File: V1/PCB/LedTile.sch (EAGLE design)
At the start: 71 parts, among them U1 BME280, U2 TSL2561T

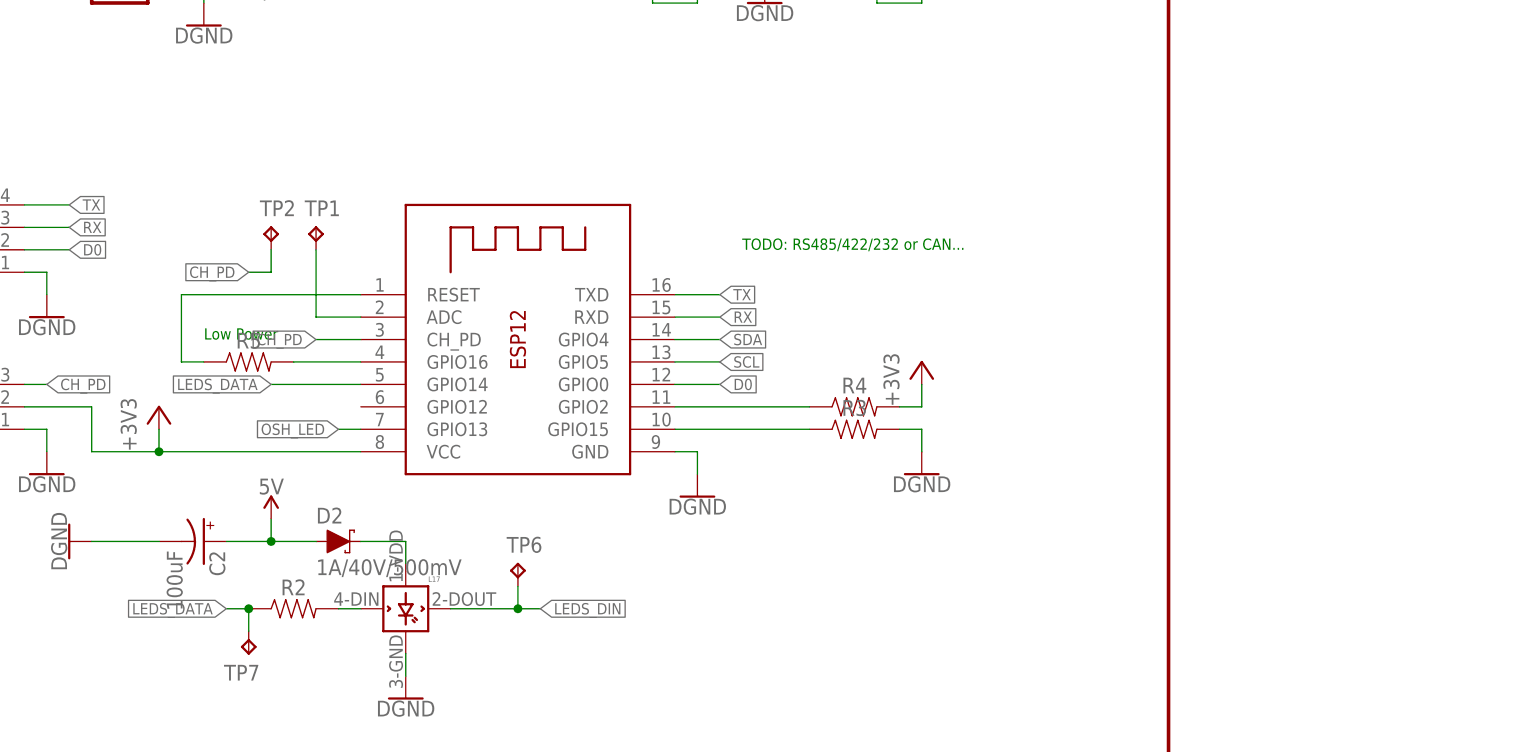
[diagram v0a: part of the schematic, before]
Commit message: V1.1 as sent to DirtyPCBs.
Added pullups required for ESP-12E
Added reset button option
Modified LED footprints to give a bigger area for soldering
Changed connectors for tile2tile to 5 pin SIL with reversable connections.
Added "compute board" pin headers to allow a behing board to have ESP on in future designs.
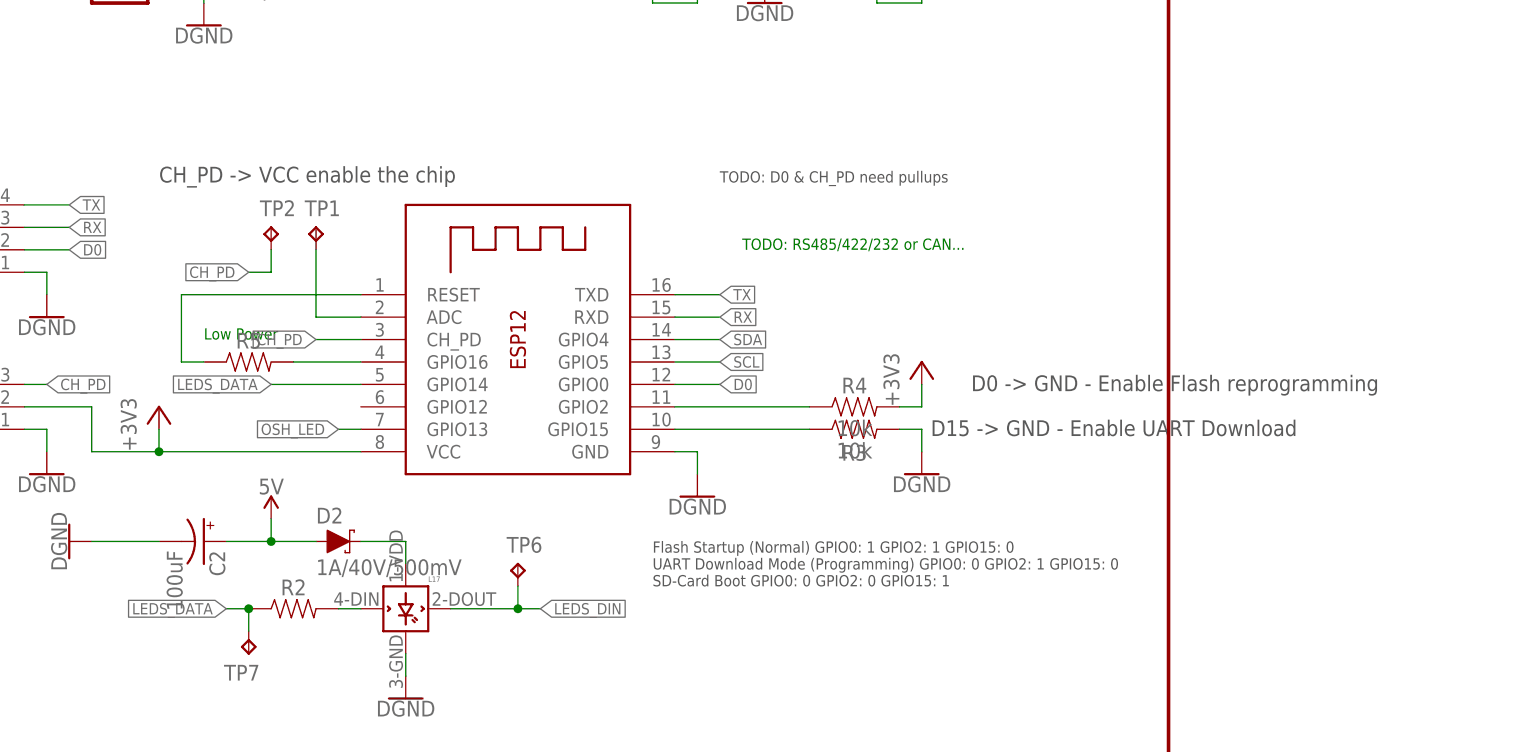
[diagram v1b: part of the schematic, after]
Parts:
- R3, R4: value (none) -> 10k
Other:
- note added: "CH_PD -> VCC enable the chip"
- note added: "D0 -> GND - Enable Flash reprogramming"
- note added: "D15 -> GND - Enable UART Download"
- note added: "Flash Startup (Normal) GPIO0: 1 GPIO2: 1 GPIO15: 0 UART Download Mode (Programming) GPIO0: 0 GPIO2: 1 GPIO15: 0 SD-Card Boot GPIO0: 0 GPIO2: 0 GPIO15: 1"
- note added: "TODO: D0 & CH_PD need pullups"
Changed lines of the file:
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@@
 <part name="SUPPLY6" library="SparkFun-PowerSymbols" deviceset="5V" device=""/>
 <part name="GND6" library="SparkFun-PowerSymbols" deviceset="DGND" device=""/>
-<part name="R3" library="SparkFun-Resistors" deviceset="RESISTOR" device="0805" value=" "/>
-<part name="R4" library="SparkFun-Resistors" deviceset="RESISTOR" device="0805" value=" "/>
+<part name="R3" library="SparkFun-Resistors" deviceset="RESISTOR" device="0805" value="10k"/>
+<part name="R4" library="SparkFun-Resistors" deviceset="RESISTOR" device="0805" value="10k"/>
 <part name="GND7" library="SparkFun-PowerSymbols" deviceset="DGND" device=""/>
 <part name="+3V2" library="supply1" deviceset="+3V3" device=""/>
@@
 <text x="200.66" y="139.7" size="1.27" layer="91">TODO: RS485/422/232 or CAN...</text>
 <text x="139.7" y="129.54" size="1.27" layer="91">Low Power</text>
+<text x="221.996" y="118.618" size="1.778" layer="97">D15 -&gt; GND - Enable UART Download</text>
+<text x="226.568" y="123.698" size="1.778" layer="97">D0 -&gt; GND - Enable Flash reprogramming</text>
+<text x="134.62" y="147.32" size="1.778" layer="97">CH_PD -&gt; VCC enable the chip</text>
+<text x="190.5" y="101.6" size="1.27" layer="97">Flash Startup (Normal) GPIO0: 1 GPIO2: 1 GPIO15: 0
+UART Download Mode (Programming) GPIO0: 0 GPIO2: 1 GPIO15: 0
+SD-Card Boot GPIO0: 0 GPIO2: 0 GPIO15: 1</text>
+<text x="198.12" y="147.32" size="1.27" layer="97">TODO: D0 &amp; CH_PD need pullups</text>
 </plain>
 <instances>
@@
 <instance part="SUPPLY6" gate="G$1" x="2.54" y="76.2"/>
 <instance part="GND6" gate="G$1" x="53.34" y="71.12"/>
-<instance part="R3" gate="G$1" x="213.36" y="119.38"/>
-<instance part="R4" gate="G$1" x="213.36" y="121.92"/>
+<instance part="R3" gate="G$1" x="213.36" y="119.38" smashed="yes">
+<attribute name="NAME" x="213.36" y="115.824" size="1.778" layer="95" font="vector" align="bottom-center"/>
+<attribute name="VALUE" x="213.36" y="117.856" size="1.778" layer="96" font="vector" align="top-center"/>
+</instance>
+<instance part="R4" gate="G$1" x="213.36" y="121.92" smashed="yes">
+<attribute name="NAME" x="213.36" y="123.444" size="1.778" layer="95" font="vector" align="bottom-center"/>
+<attribute name="VALUE" x="213.36" y="120.396" size="1.778" layer="96" font="vector" align="top-center"/>
+</instance>
 <instance part="GND7" gate="G$1" x="220.98" y="114.3"/>
 <instance part="+3V2" gate="G$1" x="220.98" y="127"/>
@@
 </schematic>
 </drawing>
+<compatibility>
+<note version="6.3" minversion="6.2.2" severity="warning">
+Since Version 6.2.2 text objects can contain more than one line,
+which will not be processed correctly with this version.
+</note>
+</compatibility>
 </eagle>
